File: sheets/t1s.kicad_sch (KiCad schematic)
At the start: 0 parts

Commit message: Schematic capture: T1S (p5) and output switch (p6-p8)
Page 5: LAN8670 with per-pin decoupling, RMII mode and PHYAD straps, the
DEC-012 line interface (C0G DC block, ACT1210E-241 choke, VETH100A1DD1
ESD, DNP 100R termination) and the 50 MHz clock feeding PHY and MCU.
Pages 6-8: one TPS2HCS08A-Q1 sheet placed three times, with the SPI
daisy chain, SNS network, VDD filter and package NTC; the root maps
each placement to OUT1..OUT6, SW1..3 and the chain nets.

Co-Authored-By: Claude Opus 5.5 <noreply@anthropic.com>
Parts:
- added C (x7): 100nF, symbol Device:C
- added C (x4): 10nF, symbol Device:C
- added C (x2): 10uF, symbol Device:C
- added D (x2): VETH100A1DD1HG3-08, DropOut_Diode_SMD:Vishay_DFN1006-2B_1.0x0.6mm, symbol DropOut_Protection:VETH100A1DD1HG3-08
- added FL: ACT1210E-241-2P-TL00, DropOut_Inductor_SMD:L_CommonModeChoke_TDK_ACT1210E_3.2x2.5mm, symbol DropOut_Inductor:ACT1210E-241-2P-TL00
- added R (x2): 33R, symbol Device:R
- added R (x11): 10k, symbol Device:R
- added R: 12.4k, symbol Device:R
- added R: 100R, symbol Device:R
- added TP: TP_MDIO0_T1S_MDIO, symbol Connector:TestPoint
- added TP: TP_INH, symbol Connector:TestPoint
- added TP: TP_MDIO0_T1S_MDC, symbol Connector:TestPoint
- added TP: TP_RESET_L, symbol Connector:TestPoint
- added TP: TP_GND, symbol Connector:TestPoint
- added TP: TP_RMII0_T1S_REF_CLK, symbol Connector:TestPoint
- added TP: TP_T1S_IRQ_L, symbol Connector:TestPoint
- added U: LAN8670D0-E_LMXVAO, DropOut_Package_DFN_QFN:Microchip_LMX_VQFN-32-1EP_5x5mm_P0.5mm_EP3.5x3.5mm, symbol DropOut_Interface:LAN8670D0-E_LMXVAO
- added Y: ECS-3225SMVQ-500-DS-TR, DropOut_Oscillator:Oscillator_SMD_ECS_LGA-4_2.5x3.2mm_P2.3mm, symbol DropOut_Timing:ECS-3225SMVQ-500-DS-TR
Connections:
- new net 3V3_MAIN: C.1, C.1, C.1, C.1, C.1, C.1, C.1, C.1, C.1, R.1, R.1, R.1, R.1, U.18 (VDDP), U.29 (VDDA), U.8 (VDDP), Y.1 (Tri-State), Y.4 (VDD)
- new net GND: C.2, C.2, C.2, C.2, C.2, C.2, C.2, C.2, C.2, C.2, C.2, D.1 (A1), D.1 (A1), R.2, R.2, R.2, R.2, R.2, R.2, R.2, R.2, TP.1, U.11 (TXER/ACMA/LINK), U.32 (WAKE_IN/WAKE_IO), U.33 (VSS), Y.2 (GND)
- new net INH: R.1, TP.1, U.1 (INH)
- new net MDIO0_T1S_MDC: TP.1, U.13 (MDC)
- new net MDIO0_T1S_MDIO: R.2, TP.1, U.14 (MDIO)
- new net RESET_L: TP.1, U.10 (~{RESET})
- new net RMII0_T1S_CRS_DV: R.1, U.20 (RXDV/CRSDV/PHYAD1)
- new net RMII0_T1S_REF_CLK: R.2, TP.1
- new net RMII0_T1S_RXD0: R.1, U.16 (RXD0/PHYAD2)
- new net RMII0_T1S_RXD1: R.1, U.19 (RXD1/PHYAD3)
- new net RMII0_T1S_RX_ER: R.2, U.21 (RXER/PHYAD0)
- new net RMII0_T1S_TXD0: U.6 (TXD0)
- new net RMII0_T1S_TXD1: U.5 (TXD1)
- new net RMII0_T1S_TX_EN: R.1, U.7 (TXEN)
- new net T1S_CMC_N: C.2, FL.2
- new net T1S_CMC_P: C.2, FL.1
- new net T1S_IRQ_L: R.2, TP.1, U.22 (~{IRQ})
- new net T1S_MODE0: R.1, U.23 (RXD2/MODE0)
- new net T1S_MODE1: R.2, U.24 (RXD3/MODE1)
- new net T1S_N: D.2 (A2), FL.3, R.2
- new net T1S_OSC_OUT: R.1, R.1, Y.3 (OUT)
- new net T1S_P: D.2 (A2), FL.4, R.1
- new net T1S_PHYAD4: R.1, U.15 (CRS/PHYAD4)
- new net T1S_PHY_N: C.1, U.31 (TRXN)
- new net T1S_PHY_P: C.1, U.30 (TRXP)
- new net T1S_RBIAS: R.1, U.26 (RBIAS)
- new net T1S_REFCLK: R.2, U.27 (XTI/REFCLKIN)
- new net VDDAU_AON: C.1, C.1, U.25 (VDDAU)
- no-connect marks 0 -> 7
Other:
- note added: "10BASE-T1S PHY, RMII, PHYAD 1 (U501)"
- note added: "50 MHz RMII reference clock to PHY and MCU (Y501)"
- note added: "DESIGN VALUES (LAN8670 DS60001573K; OPEN Alliance 10BASE-T1S; Node60 DEC-007, DEC-012) Mode straps MODE[1:0] = 10b (RMII, 50 MHz REFCLKIN): RXD3/MODE1 pulled up, RXD2/MODE0 pulled down, 10k each. PHYAD[4:0] = 00001b: RXER/PHYAD0 up; CRSDV/PHYAD1, RXD0/PHYAD2, RXD1/PHYAD3, CRS/PHYAD4 down (10k). PHYAD is a hardware strap only; the PLCA node ID is commissioned in flash (separate from PHYAD). TXEN 1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"
- note added: "PHY straps and pulls (R5xx)"
- note added: "T1S line interface: DC block, CMC, ESD, DNP termination (C5xx, FL501, D501-D502)"
- note added: "Test points"
- note added: "VDDA"
- note added: "VDDAU (always on)"
- note added: "VDDP"
- title: Node60 -> Node60 · D · 10BASE-T1S (p5)

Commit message: Swap all resistors, capacitors and test points for DropOut parts
Library bumped to 752b63c (PR #22: 83 AEC-Q200 chip resistors and MLCCs,
PR #24: passive symbol layout). Each passive is now a real part, chosen
by rule: exact value and dielectric, tolerance and voltage at least as
good, the drawn package else the next larger, then manufacturer order;
the other built sources stay in the library as alternates.

Where the library has no part in the drawn package: 10nF C0G, 4.7nF C0G,
1uF 16V and 470nF 16V 0402 -> 0603; 68nF C0G, 100nF C0G and 10uF 16V
0805 -> 1206; 32k 1% -> 0.1% (TNPW060332K0BEEA); CCAP 1uF 50V (not built)
-> 1uF 100V 1206. 0R debug links on regulator outputs use the 5 A
CRCW06030000Z0EAHP jumper.

Also fixes test points: f9af1d2 described them as swapped, but they were
still stock symbols. They are now TestPoint_Pad_D1.0mm (signals) and
Harwin S1751-46R (GND loops).

Only placeholders left: L201 / C208 (EMI filter, TBD) and J901-J903.

Co-Authored-By: Claude Opus 5.5 <noreply@anthropic.com>
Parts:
- C: footprint (none) -> DropOut_Capacitor_SMD:C_1206_3216Metric; symbol Device:C -> DropOut_Capacitor:GCM31C5C2A104JE02L; Case (none) -> 1206; DigiKey_PN (none) -> 490-GCM31C5C2A104JE02LCT-ND; MPN (none) -> GCM31C5C2A104JE02L; Manufacturer (none) -> Murata; Mouser_PN (none) -> 81-GCM31C5C2A104JE2L; Package 1206 -> (none); Placeholder PLACEHOLDER: awaiting DropOut_Resistor/DropOut_Capacitor pa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 -> (none); Temperature_Grade (none) -> AEC-Q200, -55 to +125 °C; Tolerance 5% -> ±5%
- C: footprint (none) -> DropOut_Capacitor_SMD:C_0402_1005Metric; symbol Device:C -> DropOut_Capacitor:GCM155R71H103KA55D; Case (none) -> 0402; DigiKey_PN (none) -> 490-4762-1-ND; MPN (none) -> GCM155R71H103KA55D; Manufacturer (none) -> Murata; Mouser_PN (none) -> 81-GCM155R71H103KA5D; Package 0402 -> (none); Placeholder PLACEHOLDER: awaiting DropOut_Resistor/DropOut_Capacitor pa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 -> (none); Temperature_Grade (none) -> AEC-Q200, -55 to +125 °C; Tolerance 10% -> ±10%
- C: footprint (none) -> DropOut_Capacitor_SMD:C_0402_1005Metric; symbol Device:C -> DropOut_Capacitor:GCM155R71C104KA55D; Case (none) -> 0402; DigiKey_PN (none) -> 490-4759-1-ND; MPN (none) -> GCM155R71C104KA55D; Manufacturer (none) -> Murata; Mouser_PN (none) -> 81-GCM155R71C104KA5D; Package 0402 -> (none); Placeholder PLACEHOLDER: awaiting DropOut_Resistor/DropOut_Capacitor pa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 -> (none); Temperature_Grade (none) -> AEC-Q200, -55 to +125 °C; Tolerance 10% -> ±10%
- C: footprint (none) -> DropOut_Capacitor_SMD:C_1206_3216Metric; symbol Device:C -> DropOut_Capacitor:GCM31CR71C106KA64L; Case (none) -> 1206; DigiKey_PN (none) -> 490-4793-1-ND; MPN (none) -> GCM31CR71C106KA64L; Manufacturer (none) -> Murata; Mouser_PN (none) -> 81-GCM31CR71C106KA4L; Notes (none) -> No AEC-Q200 10 uF 16 V X7R part exists in the drawn 0805 pa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; Package 0805 -> (none); Placeholder PLACEHOLDER: awaiting DropOut_Resistor/DropOut_Capacitor pa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 -> (none); Temperature_Grade (none) -> AEC-Q200, -55 to +125 °C; Tolerance 10% -> ±10%
- R: footprint (none) -> DropOut_Resistor_SMD:R_0402_1005Metric; symbol Device:R -> DropOut_Resistor:AC0402JR-0733RL; Case (none) -> 0402; DigiKey_PN (none) -> YAG3543CT-ND; MPN (none) -> AC0402JR-0733RL; Manufacturer (none) -> Yageo; Mouser_PN (none) -> 603-AC0402JR-0733RL; Package 0402 -> (none); Placeholder PLACEHOLDER: awaiting DropOut_Resistor/DropOut_Capacitor pa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 -> (none); Power (none) -> 1/16W; Temperature_Grade (none) -> AEC-Q200, -55 to +155 °C; Tolerance 5% -> ±5%; Voltage (none) -> 50V
- R: footprint (none) -> DropOut_Resistor_SMD:R_0402_1005Metric; symbol Device:R -> DropOut_Resistor:AC0402JR-0710KL; Case (none) -> 0402; DigiKey_PN (none) -> YAG3517CT-ND; MPN (none) -> AC0402JR-0710KL; Manufacturer (none) -> Yageo; Mouser_PN (none) -> 603-AC0402JR-0710KL; Package 0402 -> (none); Placeholder PLACEHOLDER: awaiting DropOut_Resistor/DropOut_Capacitor pa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 -> (none); Power (none) -> 1/16W; Temperature_Grade (none) -> AEC-Q200, -55 to +155 °C; Tolerance 5% -> ±5%; Voltage (none) -> 50V
- R: footprint (none) -> DropOut_Resistor_SMD:R_0402_1005Metric; symbol Device:R -> DropOut_Resistor:AC0402FR-0712K4L; Case (none) -> 0402; DigiKey_PN (none) -> YAG5256CT-ND; MPN (none) -> AC0402FR-0712K4L; Manufacturer (none) -> Yageo; Mouser_PN (none) -> 603-AC0402FR-0712K4L; Package 0402 -> (none); Placeholder PLACEHOLDER: awaiting DropOut_Resistor/DropOut_Capacitor pa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 -> (none); Power (none) -> 1/16W; Temperature_Grade (none) -> AEC-Q200, -55 to +155 °C; Tolerance 1% -> ±1%; Voltage (none) -> 50V
- R: footprint (none) -> DropOut_Resistor_SMD:R_0603_1608Metric; symbol Device:R -> DropOut_Resistor:AC0603FR-07100RL; Case (none) -> 0603; DigiKey_PN (none) -> YAG3561CT-ND; MPN (none) -> AC0603FR-07100RL; Manufacturer (none) -> Yageo; Mouser_PN (none) -> 603-AC0603FR-07100RL; Package 0603 -> (none); Placeholder PLACEHOLDER: awaiting DropOut_Resistor/DropOut_Capacitor pa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 -> (none); Power (none) -> 1/10W; Temperature_Grade (none) -> AEC-Q200, -55 to +155 °C; Tolerance 1% -> ±1%; Voltage (none) -> 75V
- TP: value TP_MDIO0_T1S_MDIO -> TestPoint_Pad_D1.0mm; footprint (none) -> DropOut_TestPoint:TestPoint_Pad_D1.0mm; symbol Connector:TestPoint -> DropOut_Connector:TestPoint_Pad_D1.0mm; DigiKey_PN (none) -> -; MPN (none) -> TestPoint_Pad_D1.0mm; Manufacturer (none) -> DropOut; Mouser_PN (none) -> -; Notes (none) -> PCB copper only; nothing to order. Excluded from BOM and po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; Placeholder PLACEHOLDER: awaiting DropOut test-point part (library brie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 -> (none); Type 1mm pad -> (none)
- TP: value TP_INH -> TestPoint_Pad_D1.0mm; footprint (none) -> DropOut_TestPoint:TestPoint_Pad_D1.0mm; symbol Connector:TestPoint -> DropOut_Connector:TestPoint_Pad_D1.0mm; DigiKey_PN (none) -> -; MPN (none) -> TestPoint_Pad_D1.0mm; Manufacturer (none) -> DropOut; Mouser_PN (none) -> -; Notes (none) -> PCB copper only; nothing to order. Excluded from BOM and po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; Placeholder PLACEHOLDER: awaiting DropOut test-point part (library brie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 -> (none); Type 1mm pad -> (none)
- TP: value TP_MDIO0_T1S_MDC -> TestPoint_Pad_D1.0mm; footprint (none) -> DropOut_TestPoint:TestPoint_Pad_D1.0mm; symbol Connector:TestPoint -> DropOut_Connector:TestPoint_Pad_D1.0mm; DigiKey_PN (none) -> -; MPN (none) -> TestPoint_Pad_D1.0mm; Manufacturer (none) -> DropOut; Mouser_PN (none) -> -; Notes (none) -> PCB copper only; nothing to order. Excluded from BOM and po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; Placeholder PLACEHOLDER: awaiting DropOut test-point part (library brie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 -> (none); Type 1mm pad -> (none)
- TP: value TP_RESET_L -> TestPoint_Pad_D1.0mm; footprint (none) -> DropOut_TestPoint:TestPoint_Pad_D1.0mm; symbol Connector:TestPoint -> DropOut_Connector:TestPoint_Pad_D1.0mm; DigiKey_PN (none) -> -; MPN (none) -> TestPoint_Pad_D1.0mm; Manufacturer (none) -> DropOut; Mouser_PN (none) -> -; Notes (none) -> PCB copper only; nothing to order. Excluded from BOM and po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; Placeholder PLACEHOLDER: awaiting DropOut test-point part (library brie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 -> (none); Type 1mm pad -> (none)
- TP: value TP_GND -> S1751-46R; footprint (none) -> DropOut_TestPoint:TestPoint_Harwin_S1751; symbol Connector:TestPoint -> DropOut_Connector:S1751-46R; DigiKey_PN (none) -> 952-1478-1-ND; MPN (none) -> S1751-46R; Manufacturer (none) -> Harwin; Mouser_PN (none) -> 855-S1751-46R; Notes (none) -> Ground test point (probe loop) for a scope ground spring or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; Placeholder PLACEHOLDER: awaiting DropOut test-point part (library brie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 -> (none); Temperature_Grade (none) -> -55 to +125 °C; Type probe loop -> (none)
- TP: value TP_RMII0_T1S_REF_CLK -> TestPoint_Pad_D1.0mm; footprint (none) -> DropOut_TestPoint:TestPoint_Pad_D1.0mm; symbol Connector:TestPoint -> DropOut_Connector:TestPoint_Pad_D1.0mm; DigiKey_PN (none) -> -; MPN (none) -> TestPoint_Pad_D1.0mm; Manufacturer (none) -> DropOut; Mouser_PN (none) -> -; Notes (none) -> PCB copper only; nothing to order. Excluded from BOM and po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; Placeholder PLACEHOLDER: awaiting DropOut test-point part (library brie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 -> (none); Type 1mm pad -> (none)
- TP: value TP_T1S_IRQ_L -> TestPoint_Pad_D1.0mm; footprint (none) -> DropOut_TestPoint:TestPoint_Pad_D1.0mm; symbol Connector:TestPoint -> DropOut_Connector:TestPoint_Pad_D1.0mm; DigiKey_PN (none) -> -; MPN (none) -> TestPoint_Pad_D1.0mm; Manufacturer (none) -> DropOut; Mouser_PN (none) -> -; Notes (none) -> PCB copper only; nothing to order. Excluded from BOM and po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; Placeholder PLACEHOLDER: awaiting DropOut test-point part (library brie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 -> (none); Type 1mm pad -> (none)

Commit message: DEC-017: T1S bus pass-through and relay-switched termination
The user asked for a second T1S connector so a downstream node can join
the bus, and a termination that can be switched between bus end and
mid-bus (2026-10-28).

- p9: J912, a second ATM13-2P-BM04 in parallel with J903
- p5: R502 (single 100R, not fitted) replaced by the OPEN Alliance
  split termination: latching relay K501 (Omron G6KU-2F-Y-T1-TRS DC3,
  +125 °C) selects 49.9R (end, SET) or 1.5k (drop, RESET) legs to a
  centre tap with 100nF || 100k; Q501/Q502 (DMC2710UVQ-7) half-bridges
  drive the coil from 3V3_MAIN
- p4/root: PTD0 -> T1S_TERM_END, PTD1 -> T1S_TERM_DROP
- Library pinned to dropout-kicad-library PR #37 head db07592; the new
  DropOut_Relay / DropOut_Relay_SMD libraries are in the library tables
- DEC-017, parts, GATE-NET-02 (switched termination), GATE-NET-01 wake
  test in both states, firmware and network pages, GATE-MCU-01 addendum

Co-Authored-By: Claude Opus 5.5 <noreply@anthropic.com>
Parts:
- removed R: 100R, DropOut_Resistor_SMD:R_0603_1608Metric, symbol DropOut_Resistor:AC0603FR-07100RL
- added C: 100nF, DropOut_Capacitor_SMD:C_0805_2012Metric, symbol DropOut_Capacitor:CGA4J2X7R2A104K125AA
- added K: G6KU-2F-Y-T1-TRS_DC3, DropOut_Relay_SMD:Relay_DPDT_Omron_G6K-2F-Y, symbol DropOut_Relay:G6KU-2F-Y-T1-TRS_DC3
- added Q (x2): DMC2710UVQ-7, DropOut_Package_TO_SOT_SMD:Diodes_SOT-563, symbol DropOut_PowerSwitch:DMC2710UVQ-7
- added R (x2): 49.9R, DropOut_Resistor_SMD:R_1206_3216Metric, symbol DropOut_Resistor:CRCW120649R9FKEAHP
- added R (x2): 100k, DropOut_Resistor_SMD:R_0402_1005Metric, symbol DropOut_Resistor:ERJ-2RKF1003X
- added R: 100k, DropOut_Resistor_SMD:R_0805_2012Metric, symbol DropOut_Resistor:AC0805FR-07100KL
- added R (x2): 1.5k, DropOut_Resistor_SMD:R_1206_3216Metric, symbol DropOut_Resistor:CRCW12061K50FKEA
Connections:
- net 3V3_MAIN: now also Q.4 (S2), Q.4 (S2)
- net GND: now also C.2, Q.1 (S1), Q.1 (S1), R.2, R.2, R.2
- net T1S_N: now also K.6 (COM2)
- net T1S_P: now also K.3 (COM1)
- new net T1S_N_DROP: K.7 (RST2), R.2
- new net T1S_N_END: K.5 (SET2), R.2
- new net T1S_P_DROP: K.2 (RST1), R.2
- new net T1S_P_END: K.4 (SET1), R.2
- new net T1S_TERM_COIL_R: K.8 (R+), Q.3 (D2), Q.6 (D1)
- new net T1S_TERM_COIL_S: K.1 (S+), Q.3 (D2), Q.6 (D1)
- new net T1S_TERM_CT: C.1, R.1, R.1, R.1, R.1, R.1
- new net T1S_TERM_DROP: Q.2 (G1), Q.5 (G2), R.1
- new net T1S_TERM_END: Q.2 (G1), Q.5 (G2), R.1
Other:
- note added: "DEC-017 (OPEN Alliance 10BASE-T1S impl. spec 6.4.1; Microchip AN1718 rev D). Relay holds its state with no power. SET (pin 1 +, pin 8 -) = END NODE: COM-SET closed, 49.9R 1 % legs (R517, R519) -> 100R across the pair. RESET (factory state) = DROP NODE: COM-RST closed, 1.5k legs (R516, R518) = common-mode termination. Centre tap: C514 100nF 100V || R520 100k to GND. Contact resistance 100 mOhm max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"
- note added: "Switched bus termination and relay driver (K501, Q501-Q502, R516-R522, C514)"
- note added: "T1S line interface: DC block, CMC, ESD (C5xx, FL501, D501-D502)"
- note removed: "T1S line interface: DC block, CMC, ESD, DNP termination (C5xx, FL501, D501-D502)"

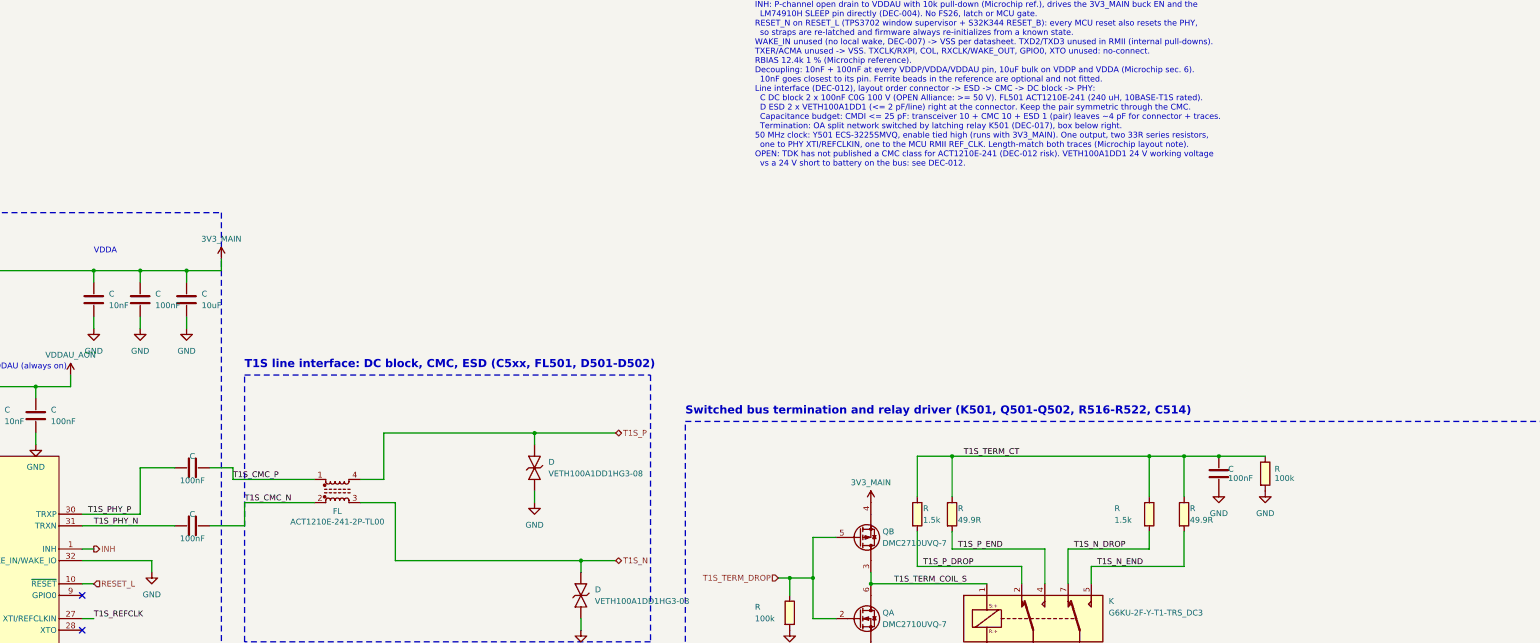
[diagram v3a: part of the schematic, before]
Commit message: DEC-012 rev. B: DC block on the connector side of the choke
Microchip AN1718 rev. D (the LAN8670 data sheet's line-interface
reference), OPEN Alliance's implementation spec (Figure 4) and both
Microchip LAN8670 evaluation boards order the line interface
connector -> ESD -> termination -> DC block -> CMC -> PHY. Node60 had
the choke on the connector side. The user approved the swap on
2026-10-29.

- p5: FL501 moved next to the PHY, C511/C512 to the bus side; no part
  changes; windings unchanged (1-4 P, 2-3 N)
- DEC-012 rev. B with the old order as a rejected option; layout notes
  on p5, p9 and in DEC-017 follow
- AN1718 and the two evaluation board schematics archived in
  dropout-vendor-docs (d4bfad3)

Co-Authored-By: Claude Opus 5.5 <noreply@anthropic.com>
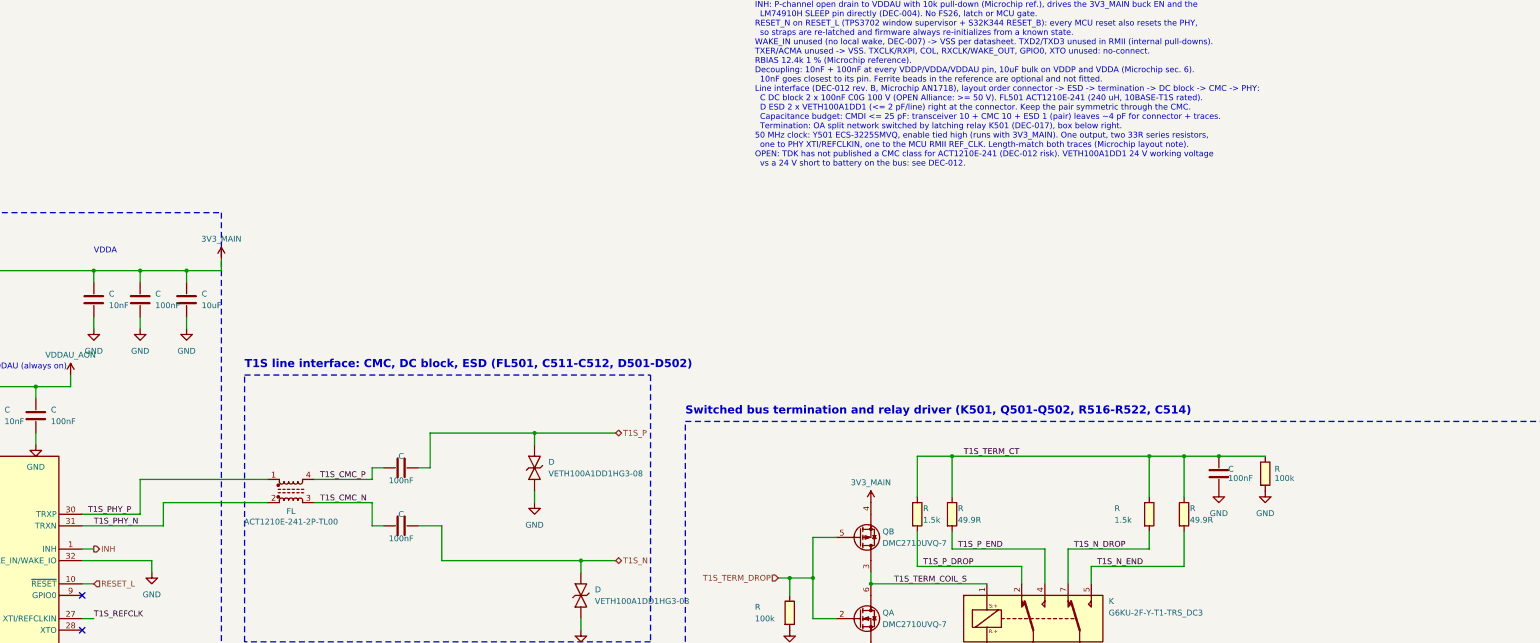
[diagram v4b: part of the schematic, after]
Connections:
- net T1S_CMC_N: now also C.1, FL.3; no longer C.2, FL.2
- net T1S_CMC_P: now also C.1, FL.4; no longer C.2, FL.1
- net T1S_N: now also C.2; no longer FL.3
- net T1S_P: now also C.2; no longer FL.4
- net T1S_PHY_N: now also FL.2; no longer C.1
- net T1S_PHY_P: now also FL.1; no longer C.1
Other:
- note added: "T1S line interface: CMC, DC block, ESD (FL501, C511-C512, D501-D502)"
- note removed: "T1S line interface: DC block, CMC, ESD (C5xx, FL501, D501-D502)"
- moved on the sheet: C, FL
